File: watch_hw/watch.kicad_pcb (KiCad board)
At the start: 6 copper layers, 38 x 40 mm, 61 parts, among them J1 2130830005, J2 FH19C-7S-0.5SH, M1 VZ43FC1B5640005L, SW1 TL6340AF160Q, SW2 TL6340AF160Q, U1 NRF52833-QDAA, U2 nPM1100-QD, U3 MAX17048G+, U4 BMA456, U5 DRV2603, U6 LIS3MDL, Y1 32MHz, Y2 32.768kHz

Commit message: Start watch v1 layout
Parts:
- removed AE1: 2450AT18D0100001, watch:ANTENNA_2450AT18D0100001
- removed C15, C17, C28: 1uF, Capacitor_SMD:C_0402_1005Metric_Pad0.74x0.62mm_HandSolder
- removed C16: 47nF, Capacitor_SMD:C_0402_1005Metric_Pad0.74x0.62mm_HandSolder
- removed C26, C27, C29: 0.1uF, Capacitor_SMD:C_0402_1005Metric_Pad0.74x0.62mm_HandSolder
- removed L2: 15nH, Inductor_SMD:L_0402_1005Metric_Pad0.77x0.64mm_HandSolder
- removed L3: 4.7nF, Inductor_SMD:L_0402_1005Metric_Pad0.77x0.64mm_HandSolder
- removed L4: 2.2nH, Inductor_SMD:L_0402_1005Metric_Pad0.77x0.64mm_HandSolder
- removed M1: VZ43FC1B5640005L, watch:VZ43FC1B5640005L
- removed R1, R2: 5.1k, Resistor_SMD:R_0402_1005Metric_Pad0.72x0.64mm_HandSolder
- removed the REF** at (140.0, 100.0)
- removed U5: DRV2603, watch:DRV2603RUN
- removed U6: LIS3MDL, watch:LIS3MDLTR
- removed Y1: 32MHz, watch:XTAL_ECX-1637B2
- removed Y2: 32.768kHz, watch:XTAL_SC32S
- added J3: Conn_ARM_SWD_TagConnect_TC2030-NL, Connector:Tag-Connect_TC2030-IDC-NL_2x03_P1.27mm_Vertical, F.Cu at (139.9, 108.8)
- added TP4: TestPoint, TestPoint:TestPoint_Keystone_5015_Micro_Mini, F.Cu at (186.3, 90.2)
- added TP5: TestPoint, TestPoint:TestPoint_Keystone_5015_Micro_Mini, F.Cu at (192.7, 107.3)
- added TP6: TestPoint, TestPoint:TestPoint_Keystone_5015_Micro_Mini, F.Cu at (192.7, 111.0)
- added X1: NX2016SA-32M, Crystal:Crystal_SMD_2016-4Pin_2.0x1.6mm, F.Cu at (153.6, 101.5)
- added X2: NX2012_32K768, Crystal:Crystal_SMD_2012-2Pin_2.0x1.2mm_HandSoldering, F.Cu at (146.5, 115.4)
- BT1, SW1, SW2: moved to F.Cu
- C1: value 9pF -> 100nF
- C10: value 4.7uF -> 100nF
- C11: value 0.1uF -> 4.7uF
- C12: value 820pF -> 100nF
- C13: value 100pF -> 10pF
- C14: value 0.1uF -> 10pF
- C2: value 9pF -> 100pF
- C3: value 10pF -> 100nF
- C4: value 1pF -> 100nF
- C5: value 1.2pF -> 100nF
- C6: value 10pF -> 4.7uF
- C7: value 0.1uF -> 10nF
- C8: value 4.7uF -> 1uF
- J1: value 2130830005 -> USB_B_Micro; footprint watch:MOLEX_2130830005 -> watch:UJ2-MIBH-4-SMT-TR-67; moved to F.Cu
- J2: value FH19C-7S-0.5SH -> FH19C-7S-0.5SH(10); moved to F.Cu
- L1: footprint Inductor_SMD:L_0805_2012Metric_Pad1.05x1.20mm_HandSolder -> Inductor_SMD:L_0805_2012Metric_Pad1.15x1.40mm_HandSolder
- TP1: value SWDCLK -> TestPoint; footprint TestPoint:TestPoint_THTPad_D1.0mm_Drill0.5mm -> TestPoint:TestPoint_Keystone_5015_Micro_Mini; moved to F.Cu
- TP2: value SWDIO -> TestPoint; footprint TestPoint:TestPoint_THTPad_D1.0mm_Drill0.5mm -> TestPoint:TestPoint_Keystone_5015_Micro_Mini; moved to F.Cu
- TP3: value RESET -> TestPoint; footprint TestPoint:TestPoint_THTPad_D1.0mm_Drill0.5mm -> TestPoint:TestPoint_Keystone_5015_Micro_Mini; moved to F.Cu
- U1: value NRF52833-QDAA -> STM32WB55CGUx; footprint watch:nRF52833-QD -> Package_DFN_QFN:QFN-48-1EP_7x7mm_P0.5mm_EP3.5x3.5mm
- U2: footprint watch:nPM1100-QD -> Package_DFN_QFN:QFN-24-1EP_4x4mm_P0.5mm_EP2.5x2.5mm
- moved R3 78.1 mm to (204.1, 71.5), turned to 0 degrees
- moved R4 75.7 mm to (204.1, 73.5), turned to 0 degrees
- moved J2 66.0 mm to (206.0, 94.9)
- moved TP1 64.0 mm to (186.3, 79.0), turned to 0 degrees
- moved TP2 62.5 mm to (186.3, 82.7), turned to 0 degrees
- moved TP3 61.7 mm to (186.3, 86.5), turned to 0 degrees
- moved C24 59.7 mm to (203.4, 111.5), turned to 0 degrees
- moved C25 59.6 mm to (203.4, 113.5), turned to 0 degrees
- moved C22 25.1 mm to (156.8, 93.2), turned to 90 degrees
- moved C6 25.0 mm to (157.1, 108.2), turned to -90 degrees
- moved C8 22.7 mm to (151.7, 115.7), turned to 0 degrees
- moved U4 22.4 mm to (154.0, 92.0), turned to 0 degrees
- moved C23 22.2 mm to (156.8, 90.7), turned to -90 degrees
- moved C11 20.6 mm to (151.1, 101.5), turned to -90 degrees
- moved BT1 20.2 mm to (143.5, 84.5), turned to -90 degrees
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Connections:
- C1 pad 1: GND -> VDD
- C1 pad 2: Net-(U1-XC1) -> GND
- C10 pad 1: /SoC/DECUSB -> VDD
- C11 pad 1: VDD -> Net-(U1-VFBSMPS)
- C12 pad 1: /SoC/DEC5 -> /SoC/NRST
- C13 pad 1: /SoC/DEC3 -> /SoC/OSC32_IN
- C14 pad 1: VDD -> /SoC/OSC32_OUT
- C2 pad 1: GND -> VDD
- C2 pad 2: Net-(U1-XC2) -> GND
- C3 pad 1: GND -> VDD
- C3 pad 2: Net-(U1-P0.00/XL1) -> GND
- C4 pad 1: Net-(U1-ANT) -> VDD
- C5 pad 1: Net-(C5-Pad1) -> VDD
- C6 pad 1: GND -> VDD
- C6 pad 2: Net-(U1-P0.01/XL2) -> GND
- C7 pad 1: /SoC/DEC1 -> VDD
- C9 pad 1: VBUS -> VDD
- L1 pad 1: Net-(U1-DCC) -> Net-(U1-VLXSMPS)
- L1 pad 2: Net-(L1-Pad2) -> Net-(U1-VFBSMPS)
- TP1 pad 1: Net-(U1-SWDCLK) -> GND
- TP2 pad 1: Net-(U1-SWDIO) -> VDD
- TP3 pad 1: Net-(U1-P0.18/~{RESET}) -> /Power/VBAT
- U1 pad 1: /SoC/DEC1 -> VDD
- U1 pad 10: VBUS -> unconnected-(U1-PA1-Pad10)
- U1 pad 11: /SoC/DECUSB -> unconnected-(U1-PA2-Pad11)
- U1 pad 12: /USB_D_N -> unconnected-(U1-PA3-Pad12)
- U1 pad 13: /USB_D_P -> unconnected-(U1-PA4-Pad13)
- U1 pad 16: Net-(U1-P0.18/~{RESET}) -> unconnected-(U1-PA7-Pad16)
- U1 pad 18: VDD -> unconnected-(U1-PA9-Pad18)
- U1 pad 19: Net-(U1-SWDIO) -> unconnected-(U1-PB2-Pad19)
- U1 pad 2: Net-(U1-P0.00/XL1) -> /SoC/OSC32_IN
- U1 pad 20: Net-(U1-SWDCLK) -> VDD
- U1 pad 21: /SoC/DEC5 -> unconnected-(U1-RF1-Pad21)
- U1 pad 22: unconnected-(U1-P0.09/NFC1-Pad22) -> GND
- U1 pad 23: unconnected-(U1-P0.10/NFC2-Pad23) -> VDD
- U1 pad 24: Net-(U1-ANT) -> /SoC/OSC_OUT
- U1 pad 25: GND -> /SoC/OSC_IN
- U1 pad 26: /SoC/DEC6 -> unconnected-(U1-AT0-Pad26)
- U1 pad 27: /SoC/DEC3 -> unconnected-(U1-AT1-Pad27)
- U1 pad 28: Net-(U1-XC1) -> unconnected-(U1-PB0-Pad28)
- U1 pad 29: Net-(U1-XC2) -> unconnected-(U1-PB1-Pad29)
- U1 pad 3: Net-(U1-P0.01/XL2) -> /SoC/OSC32_OUT
- U1 pad 30: VDD -> unconnected-(U1-PE4-Pad30)
- U1 pad 31: unconnected-(U1-P0.03/AIN1-Pad31) -> Net-(U1-VFBSMPS)
- U1 pad 32: unconnected-(U1-P0.02/AIN0-Pad32) -> GND
- U1 pad 33: unconnected-(U1-P0.28/AIN4-Pad33) -> Net-(U1-VLXSMPS)
- U1 pad 34: unconnected-(U1-P0.29/AIN5-Pad34) -> VDD
- U1 pad 35: unconnected-(U1-P0.30/AIN6-Pad35) -> VDD
- U1 pad 37: GND -> unconnected-(U1-PA11-Pad37)
- U1 pad 38: /SoC/DEC4 -> unconnected-(U1-PA12-Pad38)
- U1 pad 39: Net-(U1-DCC) -> /SoC/SWDIO
- U1 pad 41: GND -> /SoC/SWCLK
- U1 pad 7: unconnected-(U1-P0.11-Pad7) -> /SoC/NRST
- U1 pad 9: VDD -> unconnected-(U1-PA0-Pad9)
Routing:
- net VDD: track 50.3 -> 0.00 mm, vias 16 -> 0
- net GND: track 38.7 -> 0.00 mm, vias 18 -> 0
- net /Power/VBAT: track 25.3 -> 0.00 mm
- net /Power/VSYS: track 17.6 -> 0.00 mm, vias 5 -> 0
- net /SoC/DEC6: track 13.2 -> 0.00 mm, vias 2 -> 0
- net VBUS: track 10.9 -> 0.00 mm, vias 6 -> 0
- net Net-(U1-P0.01/XL2): track 8.14 -> 0.00 mm
- net Net-(U1-P0.00/XL1): track 8.12 -> 0.00 mm
- net Net-(U1-XC2): track 6.98 -> 0.00 mm
- net Net-(U1-P0.18/~{RESET}): track 6.54 -> 0.00 mm
- net Net-(M1--): track 6.45 -> 0.00 mm, vias 1 -> 0
- net Net-(U1-XC1): track 6.32 -> 0.00 mm
- net Net-(U1-SWDIO): track 5.47 -> 0.00 mm
- net /USB_D_N: track 5.02 -> 0.00 mm, vias 2 -> 0
- net Net-(U1-SWDCLK): track 4.96 -> 0.00 mm
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- removed copper zone on B.Cu, net GND
- removed copper zone on F.Cu, net GND
- removed copper zone on In1.Cu, net GND
- removed copper zone on In4.Cu, net GND
- removed copper zone on In2.Cu, net VBUS
- removed copper zone on In2.Cu, net VDD
- removed copper zone on In3.Cu, net VDD
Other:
- board size 38 x 40 mm -> 39 x 39 mm

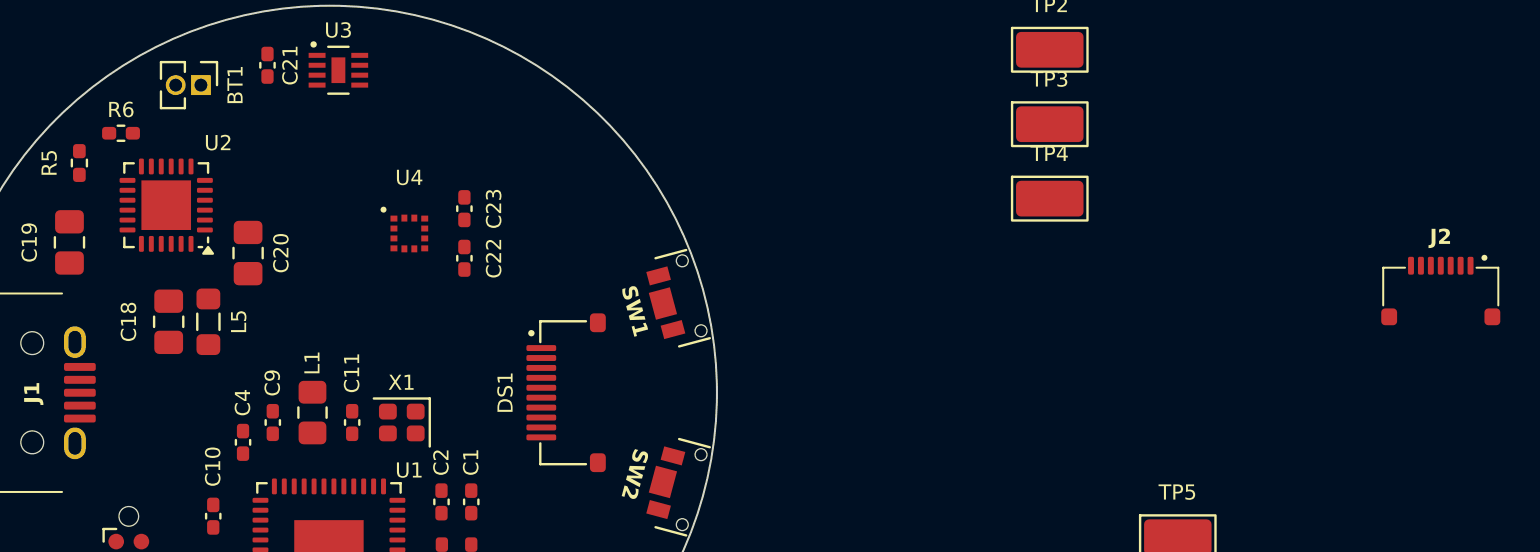
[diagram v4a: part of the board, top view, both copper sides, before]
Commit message: Add pulse sensor straight to board, fix NPM1100 symbol/footprint
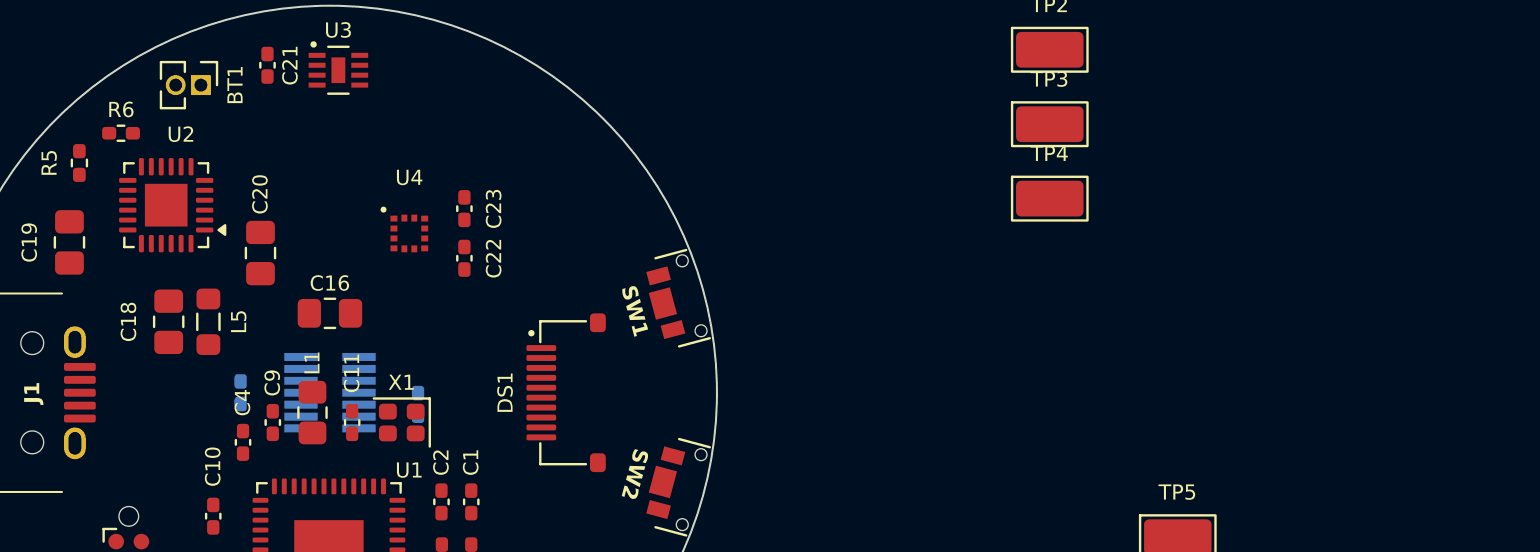
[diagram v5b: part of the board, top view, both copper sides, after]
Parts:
- removed J2: FH19C-7S-0.5SH(10), watch:FH19C-7S-0.5SH
- added C15: 1uF, Capacitor_SMD:C_0402_1005Metric_Pad0.74x0.62mm_HandSolder, B.Cu at (145.5, 100.0)
- added C16: 10uF, Capacitor_SMD:C_0805_2012Metric_Pad1.18x1.45mm_HandSolder, F.Cu at (150.0, 96.0)
- added C17: 1uF, Capacitor_SMD:C_0402_1005Metric_Pad0.74x0.62mm_HandSolder, B.Cu at (154.4, 100.6)
- added U5: MAXM86161EFD+T, watch:MAXM86161EFDT, B.Cu at (150.0, 100.0)
- U2: value nPM1100-QD -> nPM1100-QDAA; footprint Package_DFN_QFN:QFN-24-1EP_4x4mm_P0.5mm_EP2.5x2.5mm -> Package_DFN_QFN:QFN-24-1EP_4x4mm_P0.5mm_EP2.15x2.15mm
- moved C20 0.62 mm to (146.5, 93.0)
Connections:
- U2 pad 24: (no net) -> unconnected-(U2-NC-Pad24)
- U2 pad 25: (no net) -> GND

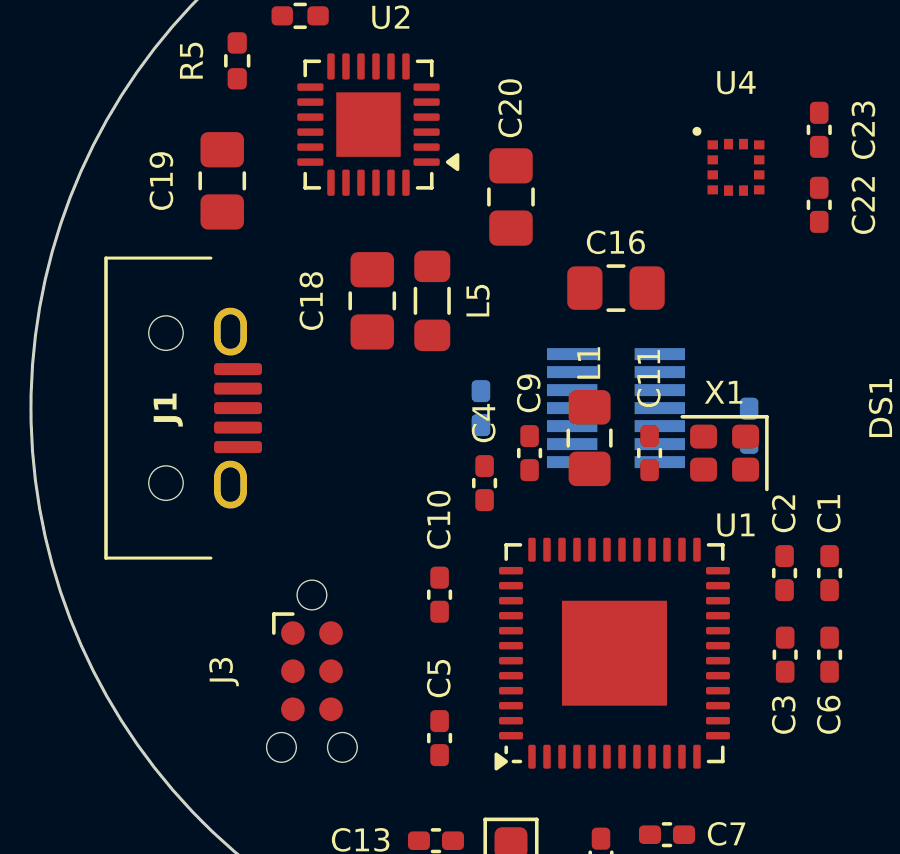
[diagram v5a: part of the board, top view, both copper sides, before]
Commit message: Route usb data
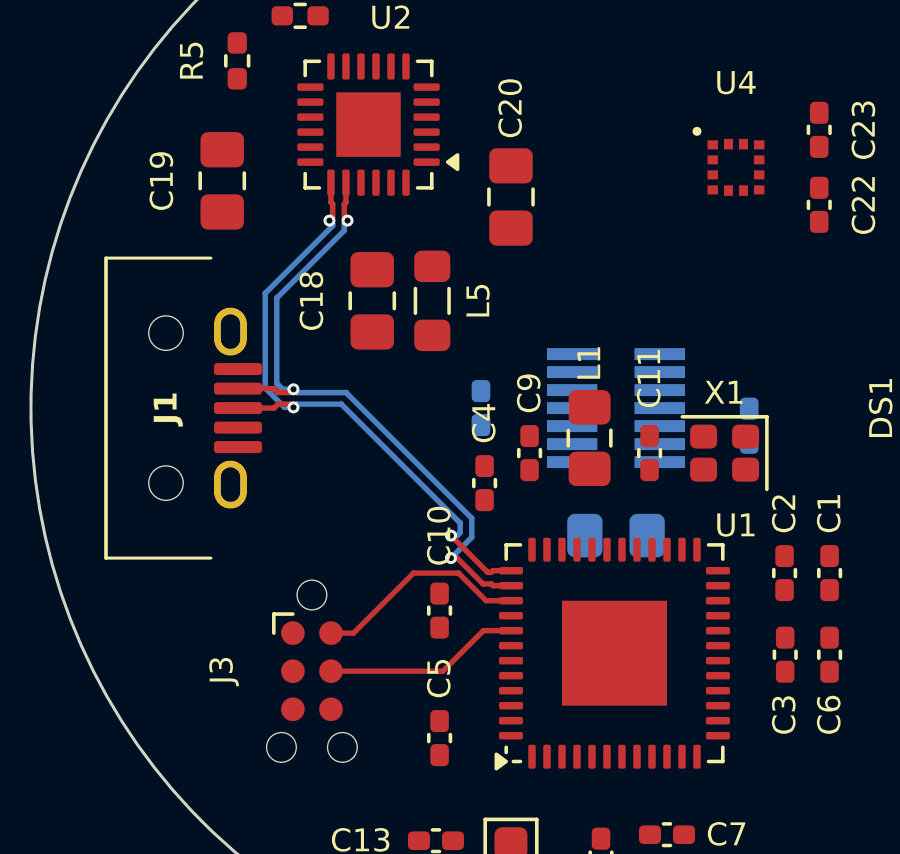
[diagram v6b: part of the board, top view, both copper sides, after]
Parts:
- C16: moved to B.Cu
- moved C16 8.25 mm to (150.0, 104.2)
- moved C10 0.53 mm to (144.1, 106.8)
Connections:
- U1 pad 37: unconnected-(U1-PA11-Pad37) -> /USB_D_N
- U1 pad 38: unconnected-(U1-PA12-Pad38) -> /USB_D_P
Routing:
- net /USB_D_P: track 0.00 -> 22.0 mm, vias 0 -> 3
- net /USB_D_N: track 0.00 -> 21.5 mm, vias 0 -> 3
- net /SoC/SWDIO: track 0.00 -> 7.21 mm
- net /SoC/SWCLK: track 0.00 -> 6.56 mm

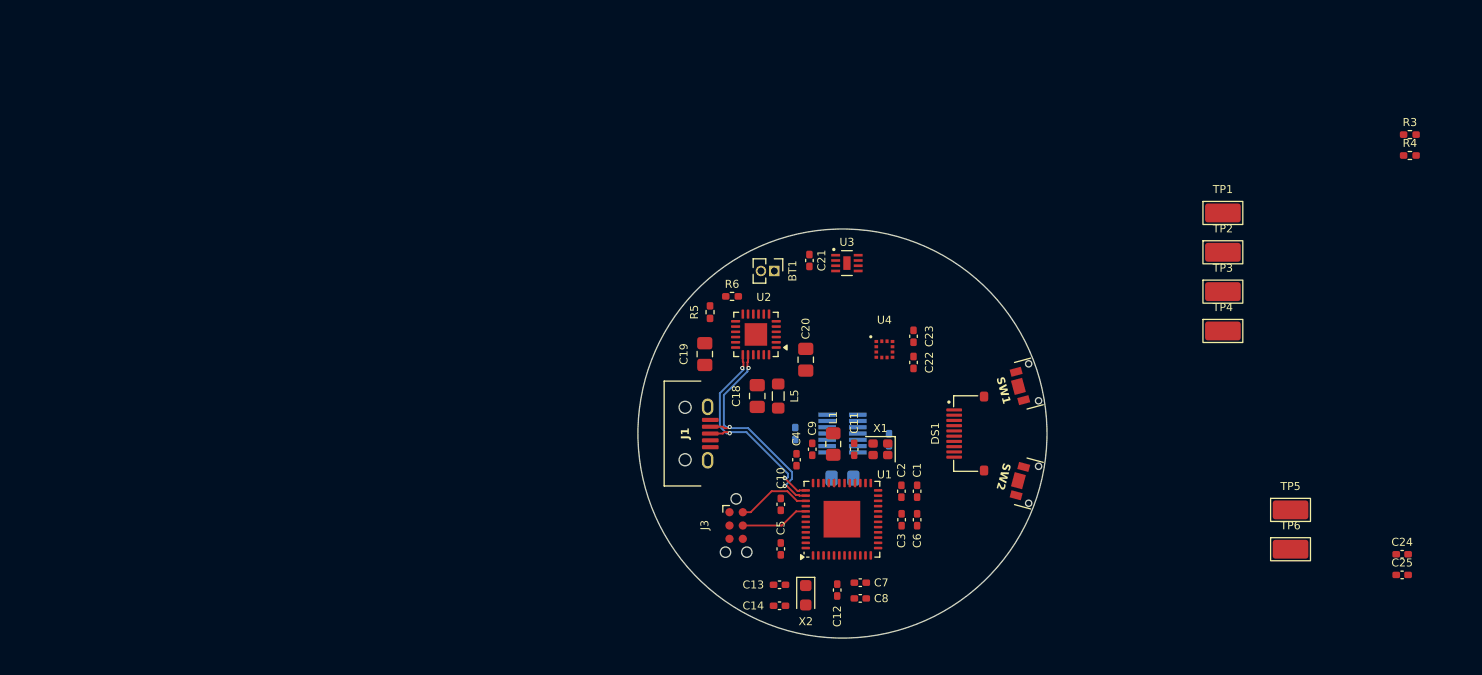
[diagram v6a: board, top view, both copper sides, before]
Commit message: route a bunch, update USB plug board edge
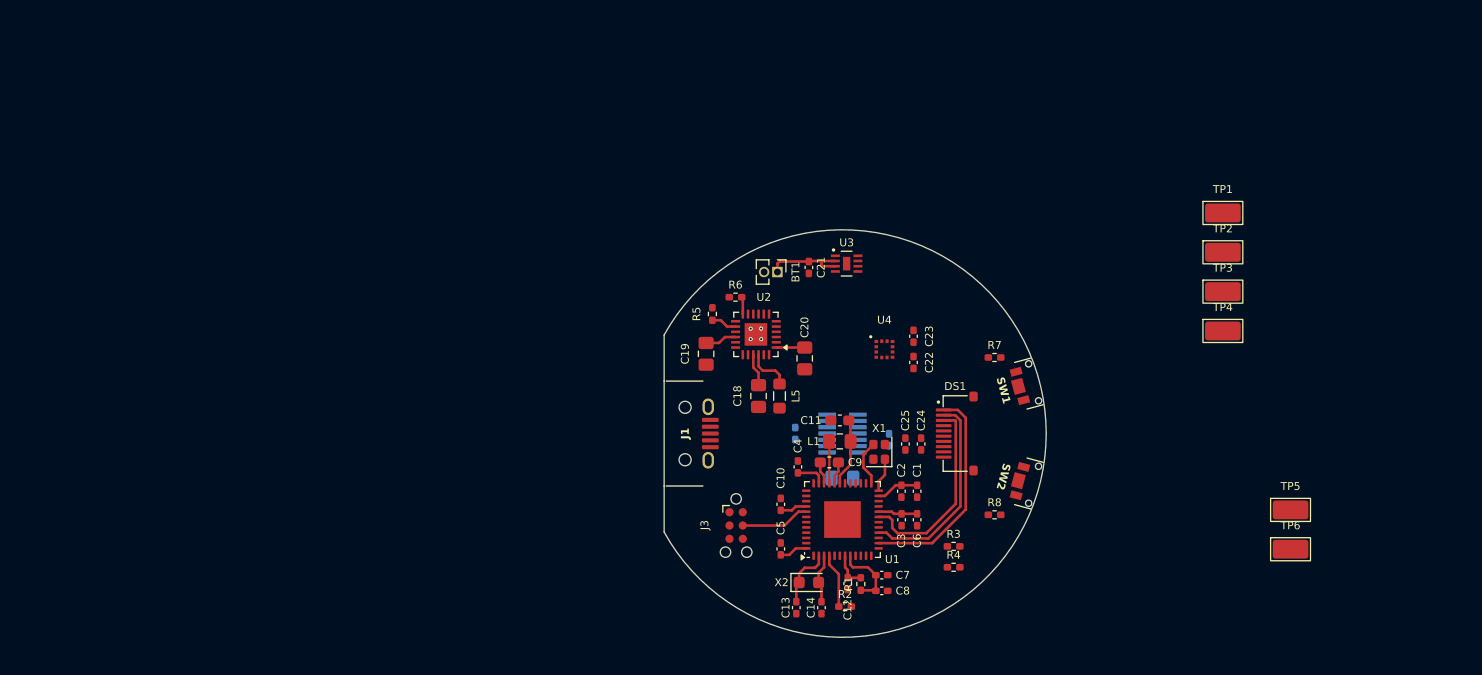
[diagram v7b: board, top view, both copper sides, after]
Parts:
- added R1: 10k, Resistor_SMD:R_0402_1005Metric_Pad0.72x0.64mm_HandSolder, F.Cu at (151.8, 114.3)
- added R2: 10k, Resistor_SMD:R_0402_1005Metric_Pad0.72x0.64mm_HandSolder, F.Cu at (150.2, 116.5)
- added R7: 10k, Resistor_SMD:R_0402_1005Metric_Pad0.72x0.64mm_HandSolder, F.Cu at (164.5, 92.8)
- added R8: 10k, Resistor_SMD:R_0402_1005Metric_Pad0.72x0.64mm_HandSolder, F.Cu at (164.5, 107.8)
- C11, C9: footprint Capacitor_SMD:C_0402_1005Metric_Pad0.74x0.62mm_HandSolder -> Capacitor_SMD:C_0603_1608Metric_Pad1.08x0.95mm_HandSolder
- moved R3 58.6 mm to (160.6, 110.8)
- moved R4 58.6 mm to (160.6, 112.8)
- moved C25 49.0 mm to (156.0, 101.0), turned to -90 degrees
- moved C24 47.0 mm to (157.5, 101.0), turned to -90 degrees
- moved C14 4.00 mm to (148.0, 116.6), turned to -90 degrees
- moved C11 3.07 mm to (149.8, 98.8), turned to 180 degrees
- moved C13 2.70 mm to (145.6, 116.6), turned to -90 degrees
- moved C7 2.17 mm to (153.8, 113.5)
- moved C8 2.17 mm to (153.8, 115.0)
- moved C9 2.05 mm to (148.8, 102.8), turned to 0 degrees
- moved X2 1.26 mm to (146.8, 114.2), turned to 0 degrees
- moved C12 1.18 mm to (150.5, 114.3)
- moved DS1 1.00 mm to (162.5, 100.0)
- moved C4 0.69 mm to (145.8, 103.2)
- moved L1 0.68 mm to (149.8, 100.8), turned to 0 degrees
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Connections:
- U1 pad 14: unconnected-(U1-PA5-Pad14) -> /Display/SCLK
- U1 pad 16: unconnected-(U1-PA7-Pad16) -> /Display/SDI
- U1 pad 19: unconnected-(U1-PB2-Pad19) -> /Display/DISP_CS
- U1 pad 4: unconnected-(U1-PH3-Pad4) -> /SoC/BOOT0
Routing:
- net VDD: track 0.00 -> 27.5 mm
- net /USB_D_P: track 22.0 -> 0.00 mm, vias 3 -> 0
- net /USB_D_N: track 21.5 -> 0.00 mm, vias 3 -> 0
- net /Display/SCLK: track 0.00 -> 20.8 mm
- net /Display/SDI: track 0.00 -> 19.3 mm
- net /Display/DISP_CS: track 0.00 -> 18.7 mm
- net /Power/VBAT: track 0.00 -> 8.23 mm
- net /SoC/SWDIO: track 7.21 -> 0.00 mm
- net Net-(U1-VFBSMPS): track 0.00 -> 6.49 mm
- net /SoC/OSC32_IN: track 0.00 -> 5.86 mm
- net /SoC/BOOT0: track 0.00 -> 5.22 mm
- net /SoC/OSC32_OUT: track 0.00 -> 4.71 mm
- net /SoC/OSC_IN: track 0.00 -> 4.40 mm
- net Net-(U2-SW): track 0.00 -> 4.32 mm
- net Net-(U1-VLXSMPS): track 0.00 -> 4.01 mm
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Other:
- board size 39 x 39 mm -> 36.4 x 38.8 mm

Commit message: route a bunch more
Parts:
- TP1, TP2, TP3, TP4, TP5, TP6: moved to B.Cu
- moved TP6 42.1 mm to (157.5, 88.0), turned to 180 degrees
- moved TP5 38.8 mm to (157.5, 91.0), turned to 180 degrees
- moved TP2 37.6 mm to (149.0, 88.0), turned to 180 degrees
- moved TP3 37.3 mm to (149.0, 85.0), turned to 180 degrees
- moved TP4 37.3 mm to (149.0, 91.0), turned to 180 degrees
- moved TP1 30.9 mm to (156.0, 85.0), turned to 180 degrees
- moved C23 5.77 mm to (151.2, 92.2), turned to 90 degrees
- moved C16 2.21 mm to (152.2, 104.4)
- moved C20 2.04 mm to (146.4, 90.8), turned to 90 degrees
- moved L5 1.87 mm to (144.4, 94.6), turned to 0 degrees
- moved R7 1.50 mm to (164.1, 94.2)
- moved C18 1.46 mm to (140.8, 95.6)
- moved C22 1.04 mm to (156.6, 92.2)
- moved BT1 0.87 mm to (144.4, 85.2)
- moved U3 0.87 mm to (151.0, 84.4)
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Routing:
- net VDD: track 27.5 -> 45.2 mm
- net /SDA: track 0.00 -> 15.5 mm, vias 0 -> 2
- net /Power/VSYS: track 3.05 -> 17.4 mm, vias 0 -> 5
- net /SCL: track 0.00 -> 12.0 mm, vias 0 -> 1
- net /Power/VBAT: track 8.23 -> 18.5 mm, vias 0 -> 1
- net VBUS: track 0.00 -> 9.40 mm
- net /BTN1: track 0.00 -> 5.71 mm
- net Net-(U5-VREF): track 0.00 -> 3.05 mm
- net Net-(U5-VLDO): track 0.00 -> 2.99 mm
- net /BTN0: track 0.00 -> 1.90 mm
- net Net-(U2-SW): track 4.32 -> 2.63 mm
- net GND: track 2.15 -> 3.75 mm, vias 4 -> 9
- net Net-(U2-DEC): track 3.11 -> 2.36 mm
- added copper zone on In1.Cu, net GND
- added copper zone on In4.Cu, net GND
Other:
- board text added: "GND"
- board text added: "SCL"
- board text added: "SDA"
- board text added: "VBAT"
- board text added: "VDD"
- board text added: "VSYS"
